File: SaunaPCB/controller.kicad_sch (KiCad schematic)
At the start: 17 parts, among them J301 KL2RM5.08, J302 KL2RM5.08, J303 KL2RM5.08, J304 KL2RM5.08, J305 B4B-ZR, J306 B5B-ZR, U301 ESP32-DEVKITC, U302 ULN2003

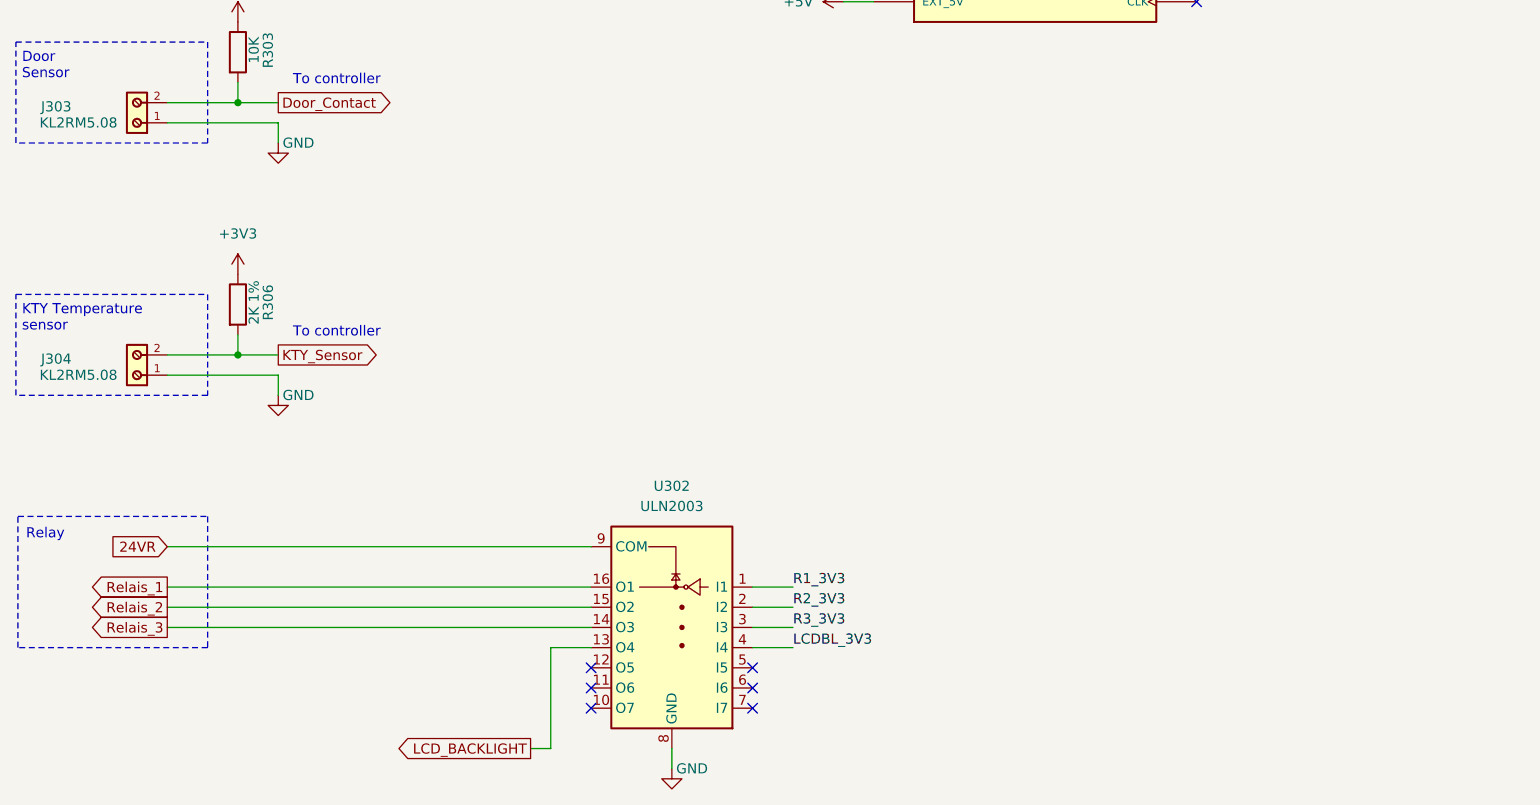
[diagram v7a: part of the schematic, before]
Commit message: Usage ULN changed Top silkscreen PCB almost ready Values Diodes changed all 1N4004 => SG1 Relay diodes changed from NB to used (for security reasons; Diode in ULN may be not powerful enough)
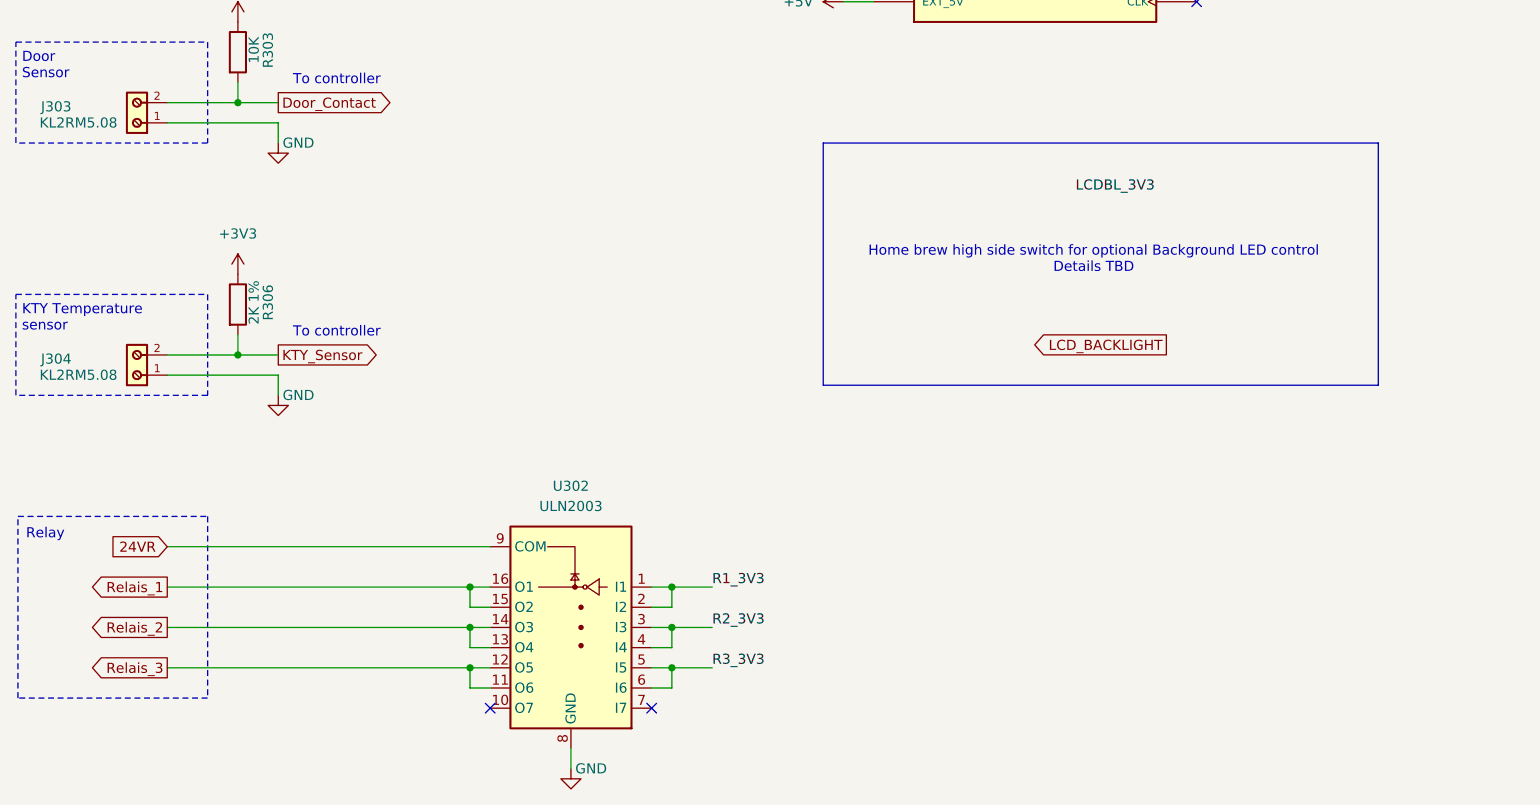
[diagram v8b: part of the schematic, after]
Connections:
- net LCDBL_3V3: no longer U302.4 (I4)
- net LCD_BACKLIGHT: no longer U302.13 (O4)
- net R1_3V3: now also U302.2 (I2)
- net R2_3V3: now also U302.3 (I3), U302.4 (I4); no longer U302.2 (I2)
- net R3_3V3: now also U302.5 (I5), U302.6 (I6); no longer U302.3 (I3)
- net Relais_1: now also U302.15 (O2)
- net Relais_2: now also U302.13 (O4), U302.14 (O3); no longer U302.15 (O2)
- net Relais_3: now also U302.11 (O6), U302.12 (O5); no longer U302.14 (O3)
- no-connect marks 20 -> 16
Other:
- note added: "Home brew high side switch for optional Background LED control Details TBD"
- moved on the sheet: U302
